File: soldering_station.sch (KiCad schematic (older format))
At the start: 50 parts

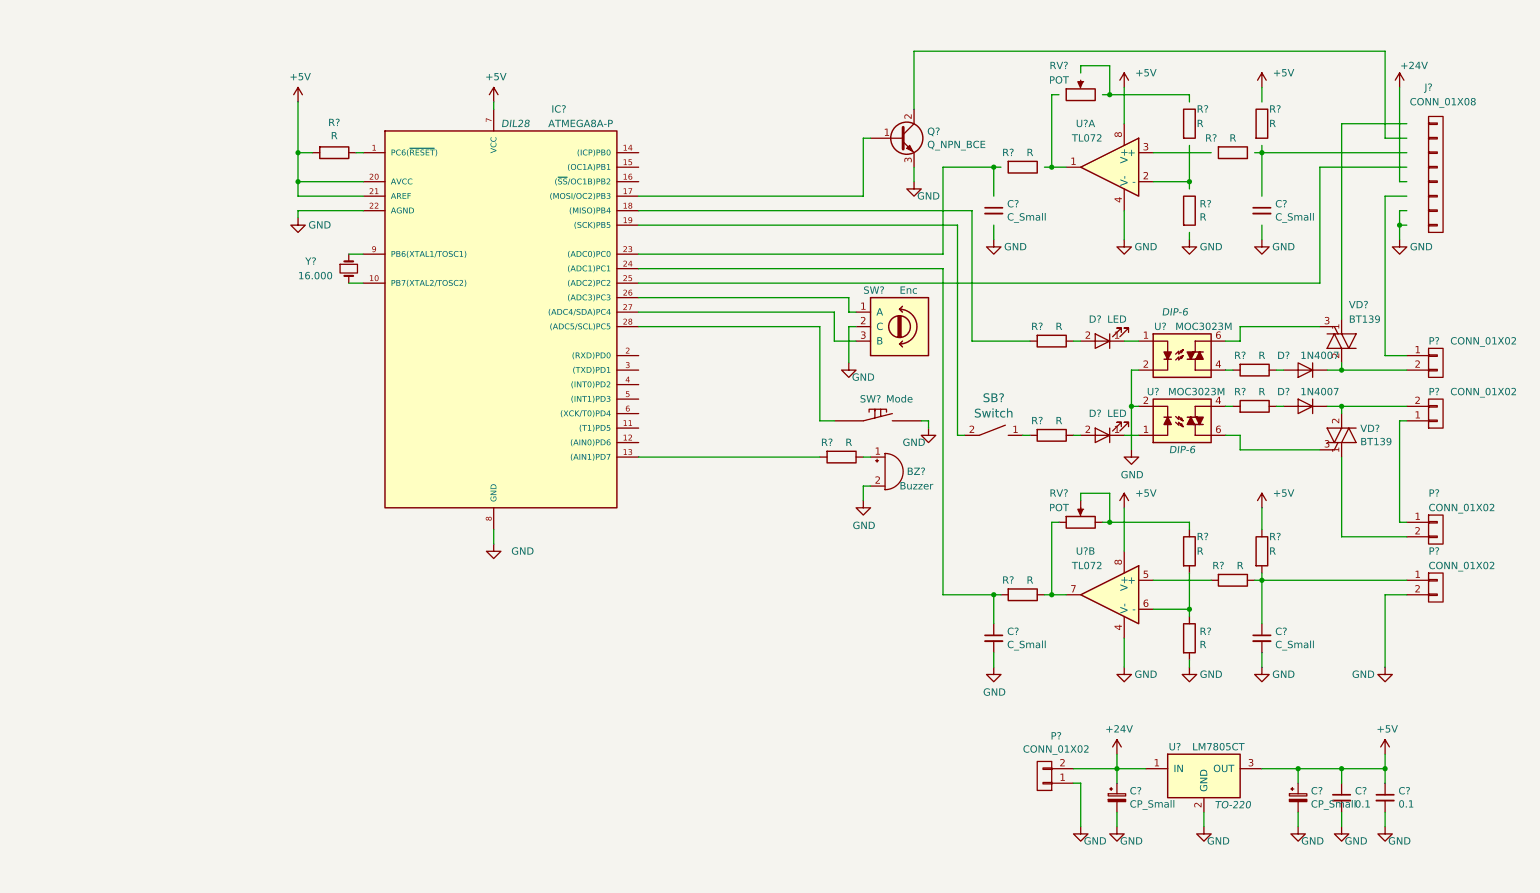
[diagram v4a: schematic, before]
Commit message: Add board
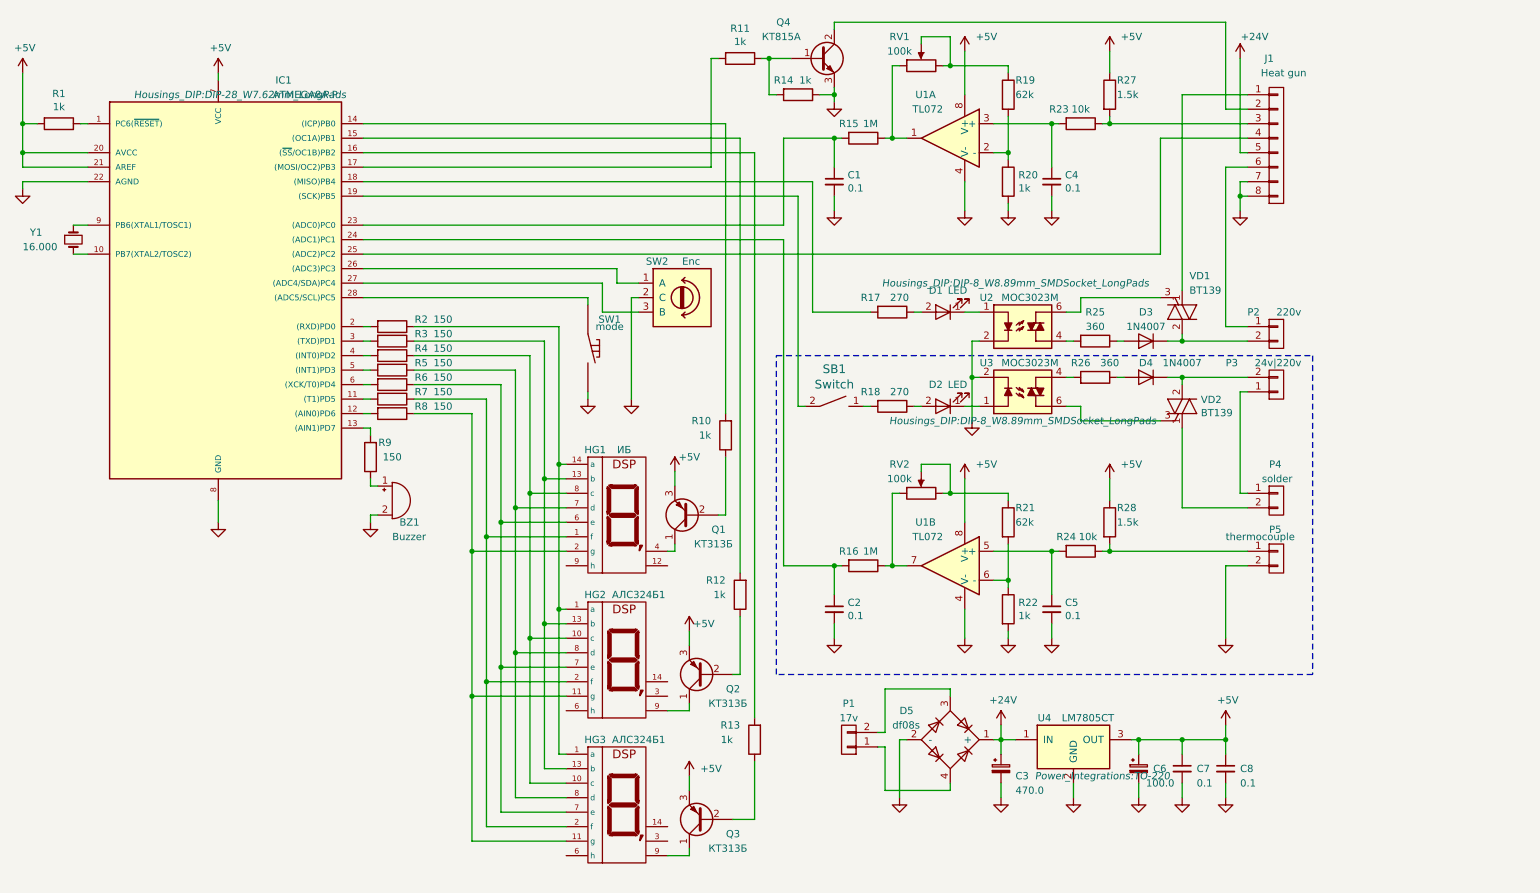
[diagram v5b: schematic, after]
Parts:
- removed P?: CONN_01X02, symbol CONN_01X02
- added D5: df08s, Oscillators:Oscillator_SMD_SeikoEpson_SG8002JA-4pin_14.0x8.7mm, symbol D_Bridge_+-AA
- added HG1: ИБ, Housings_DIP:DIP-14_W7.62mm_LongPads, symbol ИБ
- added HG2, HG3: АЛС324Б1, Housings_DIP:DIP-14_W7.62mm_LongPads, symbol АЛС324Б1
- added P1: 17v, Pin_Headers:Pin_Header_Straight_1x02_Pitch2.54mm, symbol CONN_01X02
- added Q1, Q2, Q3: КТ313Б, TO_SOT_Packages_THT:TO-92_Molded_Wide_Oval, symbol Q_PNP_CBE
- added R10, R11, R12, R13, R14: 1k, Resistors_SMD:R_0805, symbol R
- added R2, R3, R4, R5, R6, R7, R8: 150, Resistors_SMD:R_0805, symbol R
- BZ1: renamed from BZ?; footprint (none) -> Buzzers_Beepers:Buzzer_12x9.5RM7.6
- C1, C2, C4, C5: renamed from C?; value C_Small -> 0.1; footprint (none) -> Capacitors_SMD:C_0805
- C3: renamed from C?; value CP_Small -> 470.0; footprint (none) -> Capacitors_ThroughHole:CP_Radial_D8.0mm_P3.80mm
- C6: renamed from C?; value CP_Small -> 100.0; footprint (none) -> Capacitors_ThroughHole:CP_Radial_D5.0mm_P2.50mm
- C7, C8: renamed from C?; footprint (none) -> Capacitors_SMD:C_0805
- D1, D2: renamed from D?; footprint (none) -> LEDs:LED_D5.0mm
- D3, D4: renamed from D?; footprint (none) -> Diodes_ThroughHole:D_5W_P12.70mm_Horizontal
- IC1: renamed from IC?; footprint DIL28 -> Housings_DIP:DIP-28_W7.62mm_LongPads
- J1: renamed from J?; value CONN_01X08 -> Heat gun; footprint (none) -> Pin_Headers:Pin_Header_Straight_2x04_Pitch2.54mm
- P2: renamed from P?; value CONN_01X02 -> 220v; footprint (none) -> Pin_Headers:Pin_Header_Straight_1x02_Pitch3.96mm_Friction_Lock
- P3: renamed from P?; value CONN_01X02 -> 24v|220v; footprint (none) -> Pin_Headers:Pin_Header_Straight_1x02_Pitch3.96mm_Friction_Lock
- P4: renamed from P?; value CONN_01X02 -> solder; footprint (none) -> Pin_Headers:Pin_Header_Straight_1x02_Pitch3.96mm_Friction_Lock
- P5: renamed from P?; value CONN_01X02 -> thermocouple; footprint (none) -> Pin_Headers:Pin_Header_Straight_1x02_Pitch2.54mm
- Q4: renamed from Q?; value Q_NPN_BCE -> КТ815А; footprint (none) -> TO_SOT_Packages_THT:TO-126_Vertical
- R1, R20, R22: renamed from R?; value R -> 1k; footprint (none) -> Resistors_SMD:R_0805
- R15, R16: renamed from R?; value R -> 1M; footprint (none) -> Resistors_SMD:R_0805
- R17, R18: renamed from R?; value R -> 270; footprint (none) -> Resistors_SMD:R_0805
- R19, R21: renamed from R?; value R -> 62k; footprint (none) -> Resistors_SMD:R_0805
- R23, R24: renamed from R?; value R -> 10k; footprint (none) -> Resistors_SMD:R_0805
- R25, R26: renamed from R?; value R -> 360; footprint (none) -> Resistors_SMD:R_0805
- R27, R28: renamed from R?; value R -> 1.5k; footprint (none) -> Resistors_SMD:R_0805
- R9: renamed from R?; value R -> 150; footprint (none) -> Resistors_SMD:R_0805
- RV1, RV2: renamed from RV?; value POT -> 100k; footprint (none) -> Potentiometers:Potentiometer_Trimmer_ACP_CA9v_Horizontal_Px10.0mm_Py5.0mm
- SB1: renamed from SB?; footprint (none) -> Pin_Headers:Pin_Header_Straight_1x02_Pitch1.27mm
- SW1: renamed from SW?; value Mode -> mode; footprint (none) -> Buttons_Switches_THT:SW_PUSH-12mm
- SW2: renamed from SW?; footprint (none) -> Potentiometers:Potentiometer_Alps_RK09K_Horizontal
- U1: renamed from U?; footprint (none) -> Housings_DIP:DIP-8_W8.89mm_SMDSocket_LongPads
- U2, U3: renamed from U?; footprint DIP-6 -> Housings_DIP:DIP-8_W8.89mm_SMDSocket_LongPads
- U4: renamed from U?; footprint TO-220 -> Power_Integrations:TO-220
- VD1, VD2: renamed from VD?; footprint (none) -> TO_SOT_Packages_THT:TO-220_Vertical
- Y1: renamed from Y?; footprint (none) -> Crystals:Crystal_HC49-U_Vertical
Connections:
- wire segments 166 -> 220
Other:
- moved on the sheet: BZ1, C2, C3, C5, C6, C7, C8, D1, D2, D3, D4, IC1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

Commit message: Change heater gun connector
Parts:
- removed J1: Heat gun, Pin_Headers:Pin_Header_Straight_2x04_Pitch2.54mm, symbol CONN_01X08
- removed Y1: 16.000, Crystals:Crystal_HC49-U_Vertical, symbol Crystal_Small
- added P6: Fan, Pin_Headers:Pin_Header_Straight_1x02_Pitch2.54mm, symbol CONN_01X02
- added P7: thermocouple, Pin_Headers:Pin_Header_Straight_1x03_Pitch2.54mm, symbol CONN_01X03
- added P8: Heater, Pin_Headers:Pin_Header_Straight_1x02_Pitch3.96mm_Friction_Lock, symbol CONN_01X02
- D3, D4: footprint Diodes_ThroughHole:D_5W_P12.70mm_Horizontal -> Diodes_THT:D_5W_P5.08mm_Vertical_AnodeUp
- HG1: footprint Housings_DIP:DIP-14_W7.62mm_LongPads -> Displays_7-Segment:MAN3640A
- SB1: footprint Pin_Headers:Pin_Header_Straight_1x02_Pitch1.27mm -> Pin_Headers:Pin_Header_Straight_1x02_Pitch2.54mm
- U2, U3: footprint Housings_DIP:DIP-8_W8.89mm_SMDSocket_LongPads -> Housings_DIP:DIP-6_W8.89mm_SMDSocket_LongPads
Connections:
- net +24V: now also P6.1 (P1)
- net GND: now also P7.2 (P2)
- net at VD1.1 (A1): now also P8.2 (P2)
- net at Q4.2 (C): now also P6.2 (P2)
- net at R23.1, R27.2: now also P7.1 (P1)
- net at IC1.25 ((ADC2)PC2): now also P7.3 (P3)
- net at P2.1 (P1): now also P8.1 (P1)
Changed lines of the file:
@@
-$EndComp
-$Comp
-L CONN_01X08 J1
-U 1 1 5901D157
-P 9700 1450
-F 0 "J1" H 9650 2050 50  0000 C CNN
-F 1 "Heat gun" H 9750 1950 50  0000 C CNN
-F 2 "Pin_Headers:Pin_Header_Straight_2x04_Pitch2.54mm" H 9700 1450 50  0001 C CNN
-F 3 "" H 9700 1450 50  0001 C CNN
-	1    9700 1450
-	1    0    0    -1
 $EndComp
 $Comp
@@
 L GND #PWR011
 U 1 1 5912E7A7
-P 9450 1900
-F 0 "#PWR011" H 9450 1650 50  0001 C CNN
-F 1 "GND" H 9600 1850 50  0001 C CNN
-F 2 "" H 9450 1900 50  0000 C CNN
-F 3 "" H 9450 1900 50  0000 C CNN
-	1    9450 1900
+P 9350 1550
+F 0 "#PWR011" H 9350 1300 50  0001 C CNN
+F 1 "GND" H 9500 1500 50  0001 C CNN
+F 2 "" H 9350 1550 50  0000 C CNN
+F 3 "" H 9350 1550 50  0000 C CNN
+	1    9350 1550
 	1    0    0    -1
 $EndComp
@@
 F 0 "U2" H 7700 2900 50  0000 C CNN
 F 1 "MOC3023M" H 8000 2900 50  0000 C CNN
-F 2 "Housings_DIP:DIP-8_W8.89mm_SMDSocket_LongPads" H 7900 3000 50  0000 C CIN
+F 2 "Housings_DIP:DIP-6_W8.89mm_SMDSocket_LongPads" H 7900 3000 50  0000 C CIN
 F 3 "" H 7925 2700 50  0000 L CNN
 	1    7950 2700
@@
 F 0 "U3" H 7700 2950 50  0000 C CNN
 F 1 "MOC3023M" H 8000 2950 50  0000 C CNN
-F 2 "Housings_DIP:DIP-8_W8.89mm_SMDSocket_LongPads" H 7950 3350 50  0000 C CIN
+F 2 "Housings_DIP:DIP-6_W8.89mm_SMDSocket_LongPads" H 7950 3350 50  0000 C CIN
 F 3 "" H 7925 3150 50  0000 L CNN
 	1    7950 3150
@@
 F 0 "D3" H 8800 2600 50  0000 C CNN
 F 1 "1N4007" H 8800 2700 50  0000 C CNN
-F 2 "Diodes_ThroughHole:D_5W_P12.70mm_Horizontal" H 8800 2800 50  0001 C CNN
+F 2 "Diodes_THT:D_5W_P5.08mm_Vertical_AnodeUp" H 8800 2800 50  0001 C CNN
 F 3 "" H 8800 2800 50  0000 C CNN
 	1    8800 2800
@@
 F 0 "D4" H 8800 3150 50  0000 C CNN
 F 1 "1N4007" H 8550 3150 50  0000 C CNN
-F 2 "Diodes_ThroughHole:D_5W_P12.70mm_Horizontal" H 8800 3050 50  0001 C CNN
+F 2 "Diodes_THT:D_5W_P5.08mm_Vertical_AnodeUp" H 8800 3050 50  0001 C CNN
 F 3 "" H 8800 3050 50  0000 C CNN
 	1    8800 3050
@@
 F 0 "SB1" H 6650 3507 60  0000 C CNN
 F 1 "Switch" H 6650 3401 60  0000 C CNN
-F 2 "Pin_Headers:Pin_Header_Straight_1x02_Pitch1.27mm" H 6650 3250 60  0001 C CNN
+F 2 "Pin_Headers:Pin_Header_Straight_1x02_Pitch2.54mm" H 6650 3250 60  0001 C CNN
 F 3 "" H 6650 3250 60  0001 C CNN
 	1    6650 3250
@@
 L +24V #PWR024
 U 1 1 59168672
-P 9450 850
-F 0 "#PWR024" H 9450 700 50  0001 C CNN
-F 1 "+24V" H 9550 1000 50  0000 C CNN
-F 2 "" H 9450 850 50  0000 C CNN
-F 3 "" H 9450 850 50  0000 C CNN
-	1    9450 850
+P 9450 800
+F 0 "#PWR024" H 9450 650 50  0001 C CNN
+F 1 "+24V" H 9550 950 50  0000 C CNN
+F 2 "" H 9450 800 50  0000 C CNN
+F 3 "" H 9450 800 50  0000 C CNN
+	1    9450 800
 	1    0    0    -1
 $EndComp
@@
 $EndComp
 $Comp
-L Crystal_Small Y1
-U 1 1 5916E14B
-P 1400 2100
-F 0 "Y1" V 1350 1800 50  0000 L CNN
-F 1 "16.000" V 1450 1750 50  0000 L CNN
-F 2 "Crystals:Crystal_HC49-U_Vertical" H 1400 2100 50  0001 C CNN
-F 3 "" H 1400 2100 50  0000 C CNN
-	1    1400 2100
-	0    1    1    0
-$EndComp
-$Comp
 L LM7805CT U4
 U 1 1 5916F3BD
@@
 F 0 "HG1" H 5000 4450 50  0000 C CNN
 F 1 "ИБ" H 5200 4450 50  0000 C CNN
-F 2 "Housings_DIP:DIP-14_W7.62mm_LongPads" H 5195 4050 50  0001 C CNN
+F 2 "Displays_7-Segment:MAN3640A" H 5195 4050 50  0001 C CNN
 F 3 "" H 5195 4050 50  0000 C CNN
 	1    5200 4000
@@
 	9350 2700 9500 2700
 Wire Wire Line
-	9350 1600 9350 2700
+	9350 1850 9350 2700
 Connection ~ 9050 3050
 Wire Wire Line
@@
 	9350 4350 9350 4850
 Wire Wire Line
-	9050 1100 9050 2450
+	9050 1750 9050 2450
 Wire Wire Line
 	9500 4350 9350 4350
@@
 	5150 2400 5300 2400
 Wire Wire Line
-	9050 1100 9500 1100
-Wire Wire Line
-	9350 1600 9500 1600
-Wire Wire Line
-	9500 1400 8900 1400
-Wire Wire Line
-	8900 1400 8900 2200
+	9050 1750 9500 1750
+Wire Wire Line
+	9350 1850 9500 1850
+Wire Wire Line
+	9500 1500 8900 1500
+Wire Wire Line
+	8900 1500 8900 2200
 Wire Wire Line
 	8500 1300 9500 1300
 Wire Wire Line
-	9500 1700 9450 1700
-Wire Wire Line
-	9450 1700 9450 1900
-Wire Wire Line
-	9500 1800 9450 1800
-Connection ~ 9450 1800
-Wire Wire Line
-	9500 1200 9350 1200
-Wire Wire Line
-	9350 1200 9350 600
+	9500 1100 9350 1100
+Wire Wire Line
+	9350 1100 9350 600
 Wire Wire Line
 	9350 600  6650 600
@@
 	6650 1050 6650 1150
 Wire Wire Line
-	9500 1500 9450 1500
-Wire Wire Line
-	9450 1500 9450 850
-Wire Wire Line
-	1500 2000 1400 2000
-Wire Wire Line
-	1500 2200 1400 2200
+	9500 1000 9450 1000
+Wire Wire Line
+	9450 1000 9450 800
 Wire Wire Line
 	7750 5550 7900 5550
@@
 Wire Wire Line
 	3450 3400 3450 3450
+$Comp
+L CONN_01X02 P6
+U 1 1 5922F5D6
+P 9700 1050
+F 0 "P6" H 9650 1300 50  0000 L CNN
+F 1 "Fan" H 9650 1200 50  0000 L CNN
+F 2 "Pin_Headers:Pin_Header_Straight_1x02_Pitch2.54mm" H 9700 1050 50  0001 C CNN
+F 3 "" H 9700 1050 50  0000 C CNN
+	1    9700 1050
+	1    0    0    -1
+$EndComp
+$Comp
+L CONN_01X02 P8
+U 1 1 5922F6D0
+P 9700 1800
+F 0 "P8" H 9550 2000 50  0000 C CNN
+F 1 "Heater" H 9750 2000 50  0000 C CNN
+F 2 "Pin_Headers:Pin_Header_Straight_1x02_Pitch3.96mm_Friction_Lock" H 9700 1800 50  0001 C CNN
+F 3 "" H 9700 1800 50  0000 C CNN
+	1    9700 1800
+	1    0    0    1
+$EndComp
+$Comp
+L CONN_01X03 P7
+U 1 1 5922F790
+P 9700 1400
+F 0 "P7" H 9200 1600 50  0000 L CNN
+F 1 "thermocouple" H 9350 1600 50  0000 L CNN
+F 2 "Pin_Headers:Pin_Header_Straight_1x03_Pitch2.54mm" H 9700 1400 50  0001 C CNN
+F 3 "" H 9700 1400 50  0000 C CNN
+	1    9700 1400
+	1    0    0    -1
+$EndComp
+Wire Wire Line
+	9500 1400 9350 1400
+Wire Wire Line
+	9350 1400 9350 1550
 $EndSCHEMATC

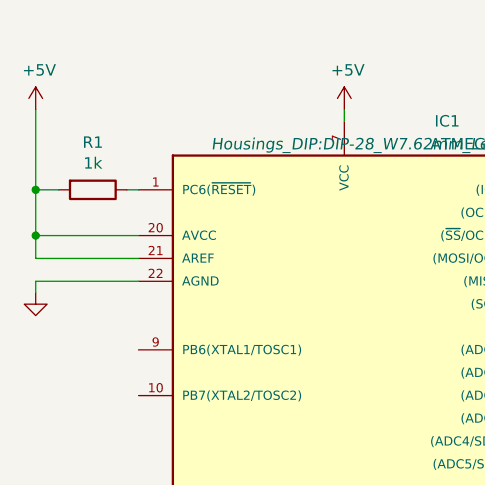
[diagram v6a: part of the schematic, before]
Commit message: Fix ADC ref pin
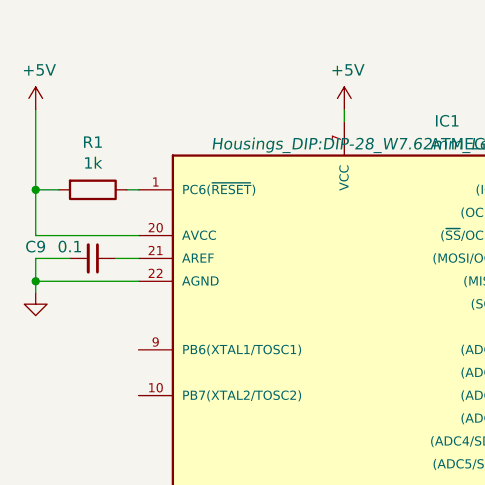
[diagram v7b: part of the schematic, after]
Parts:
- added C9: 0.1, Capacitors_SMD:C_0805, symbol C_Small
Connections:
- net +5V: no longer IC1.21 (AREF)
- net GND: now also C9.2
- new net: C9.1, IC1.21 (AREF)
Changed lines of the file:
@@
 	1500 1700 1050 1700
 Wire Wire Line
-	1050 1700 1050 1750
+	1050 1600 1050 1750
 Wire Wire Line
 	1450 1300 1500 1300
@@
 	1150 1300 1050 1300
 Wire Wire Line
-	1050 950  1050 1600
-Wire Wire Line
-	1050 1600 1500 1600
-Connection ~ 1050 1300
-Wire Wire Line
-	1500 1500 1050 1500
-Connection ~ 1050 1500
+	1050 1500 1500 1500
 Wire Wire Line
 	6300 2100 6300 4350
@@
 Wire Wire Line
 	9350 1400 9350 1550
+$Comp
+L C_Small C9
+U 1 1 59257B5A
+P 1300 1600
+F 0 "C9" V 1250 1350 50  0000 C CNN
+F 1 "0.1" V 1250 1500 50  0000 C CNN
+F 2 "Capacitors_SMD:C_0805" H 1300 1600 50  0001 C CNN
+F 3 "" H 1300 1600 50  0000 C CNN
+	1    1300 1600
+	0    1    1    0
+$EndComp
+Wire Wire Line
+	1400 1600 1500 1600
+Wire Wire Line
+	1200 1600 1050 1600
+Connection ~ 1050 1700
+Wire Wire Line
+	1050 950  1050 1500
+Connection ~ 1050 1300
 $EndSCHEMATC

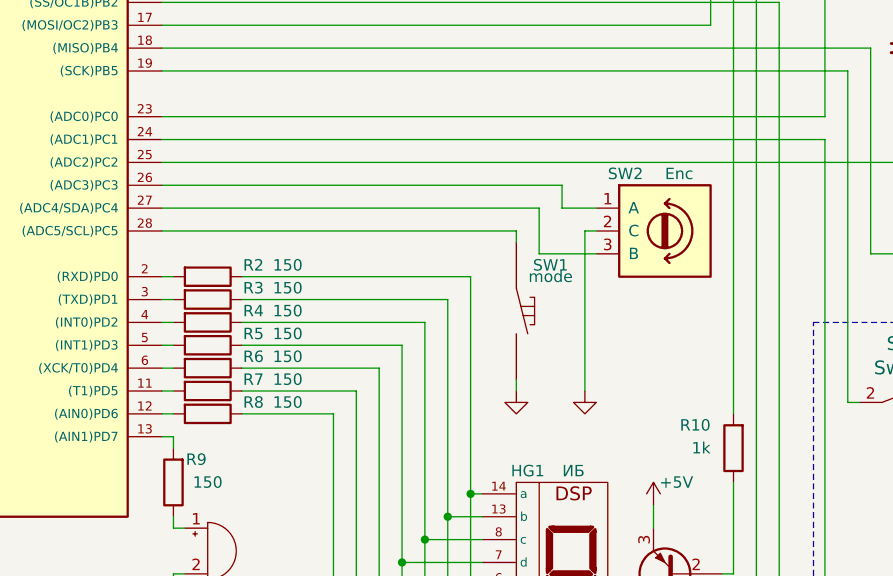
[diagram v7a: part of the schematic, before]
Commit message: Fix encoder
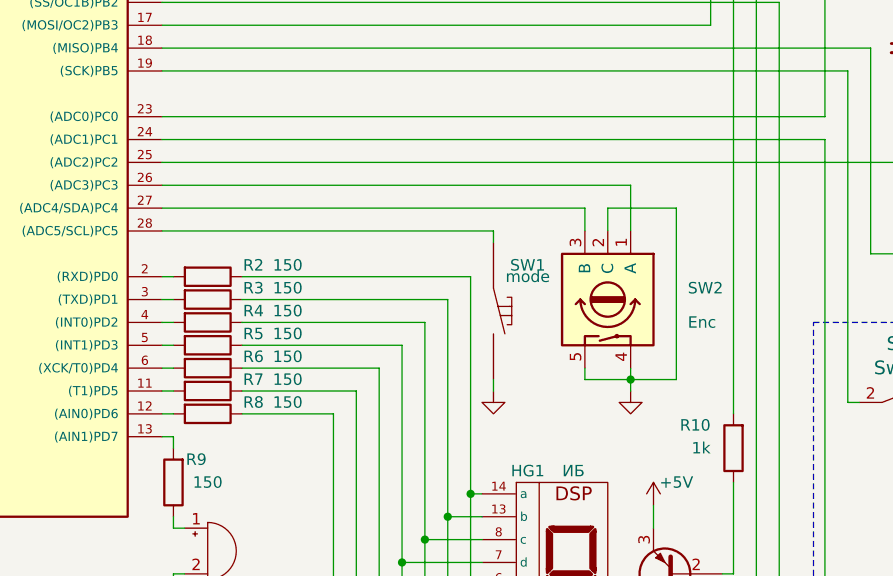
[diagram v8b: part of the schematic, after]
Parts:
- removed SW2: Enc, Potentiometers:Potentiometer_Alps_RK09K_Horizontal, symbol Rotary_Encoder
- added SW2: Enc, lib:Encoder_with_button, symbol Rotary_Encoder_Switch
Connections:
- net GND: now also SW2.2 (C), SW2.4, SW2.5
- net at IC1.26 ((ADC3)PC3): now also SW2.1 (A)
- net at IC1.27 ((ADC4/SDA)PC4): now also SW2.3 (B)
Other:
- moved on the sheet: SW1
